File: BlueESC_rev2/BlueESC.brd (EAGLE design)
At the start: 24.4 x 36 mm, 76 parts, among them Q1 BC817-40W, Q2 BC817-40W, Q3 BC817-40W, Q4 SI7370, Q5 SI7370, Q6 SI7370, Q7 SI7370, Q8 SI7370, Q9 SI7370, U1 ATMEGA168MLF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

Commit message: Placed more components on board layout.
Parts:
- removed C8: 0.1uF, SparkFun-Capacitors:0603-CAP
- R15, R16: value 1K -> 330
- moved C3 102.2 mm to (20.3, 14.0), flipped to the bottom, turned to 270 degrees
- moved C2 97.4 mm to (15.9, 34.3), flipped to the bottom
- moved C1 94.3 mm to (20.3, 25.4), flipped to the bottom, turned to 270 degrees
- moved D3 90.0 mm to (18.4, 33.7), flipped to the bottom, turned to 270 degrees
- moved D2 87.1 mm to (22.9, 26.0), flipped to the bottom, turned to 180 degrees
- moved D1 79.7 mm to (22.9, 14.6), flipped to the bottom, turned to 180 degrees
- moved R16 75.2 mm to (27.9, 33.0)
- moved U2 73.0 mm to (21.0, 7.62), turned to 270 degrees
- moved C9 72.3 mm to (21.0, 11.4)
- moved R15 67.3 mm to (24.1, 35.6)
- moved C17 59.9 mm to (14.0, 13.3), turned to 180 degrees
- moved R12 57.5 mm to (23.5, 28.6), turned to 90 degrees
- moved C16 55.3 mm to (14.0, 9.53), turned to 180 degrees
- moved R14 53.1 mm to (11.4, 29.2), turned to 270 degrees
- moved C15 51.7 mm to (14.0, 5.71), turned to 180 degrees
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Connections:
- net GND: no longer C8.2
- net VCC5V: no longer C8.1

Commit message: Added ACS71X to the schematic and board layout to measure current.
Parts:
- added C10, C8: 0.1uF, SparkFun-Capacitors:0603-CAP
- added U$15: ACS712, SparkFun-AnalogIC:SO08
- moved LOGO1 90.0 mm to (4.45, 31.8)
- moved U$4 61.1 mm to (3.17, 27.3)
- moved U$2 8.25 mm to (4.45, 5.71), flipped to the top
- moved U$1 8.08 mm to (21.6, 8.26), flipped to the top
- moved U2 5.72 mm to (21.0, 13.3)
- moved C9 5.24 mm to (19.7, 16.5)
- moved C15 3.81 mm to (10.2, 5.71)
- moved C16 3.81 mm to (10.2, 9.53)
- moved R7 1.42 mm to (5.08, 10.2), turned to 180 degrees
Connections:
- new net CURRENT_ADC: U$15.7, U1.19
- new net N$1: C8.1, U$15.6
- new net VBAT+: U$1.P$1, U$15.1, U$15.2
- net GND: now also C10.2, C8.2, U$15.5
- net VBAT: now also U$15.3, U$15.4; no longer U$1.P$1
- net VCC5V: now also C10.1, U$15.8

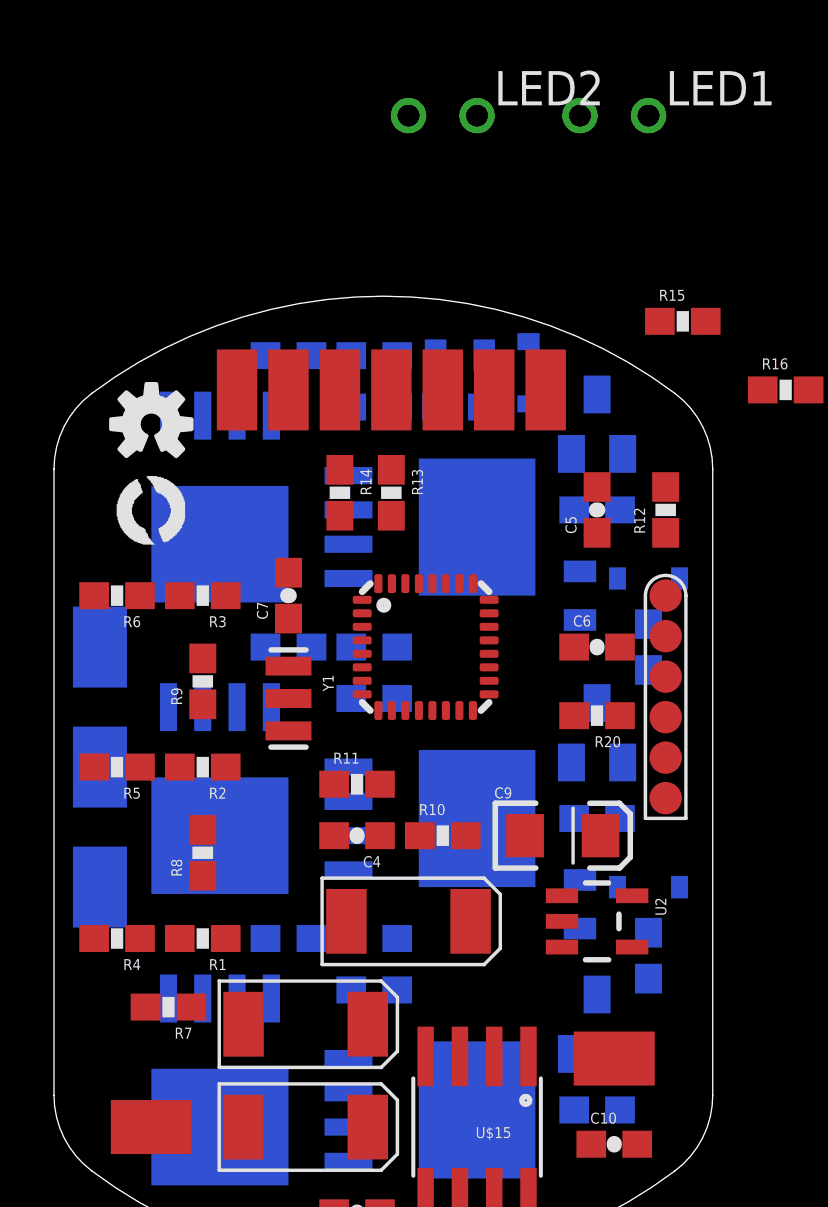
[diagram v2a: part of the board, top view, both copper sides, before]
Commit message: Updated rev3 schematic and split the schematic into two boards.
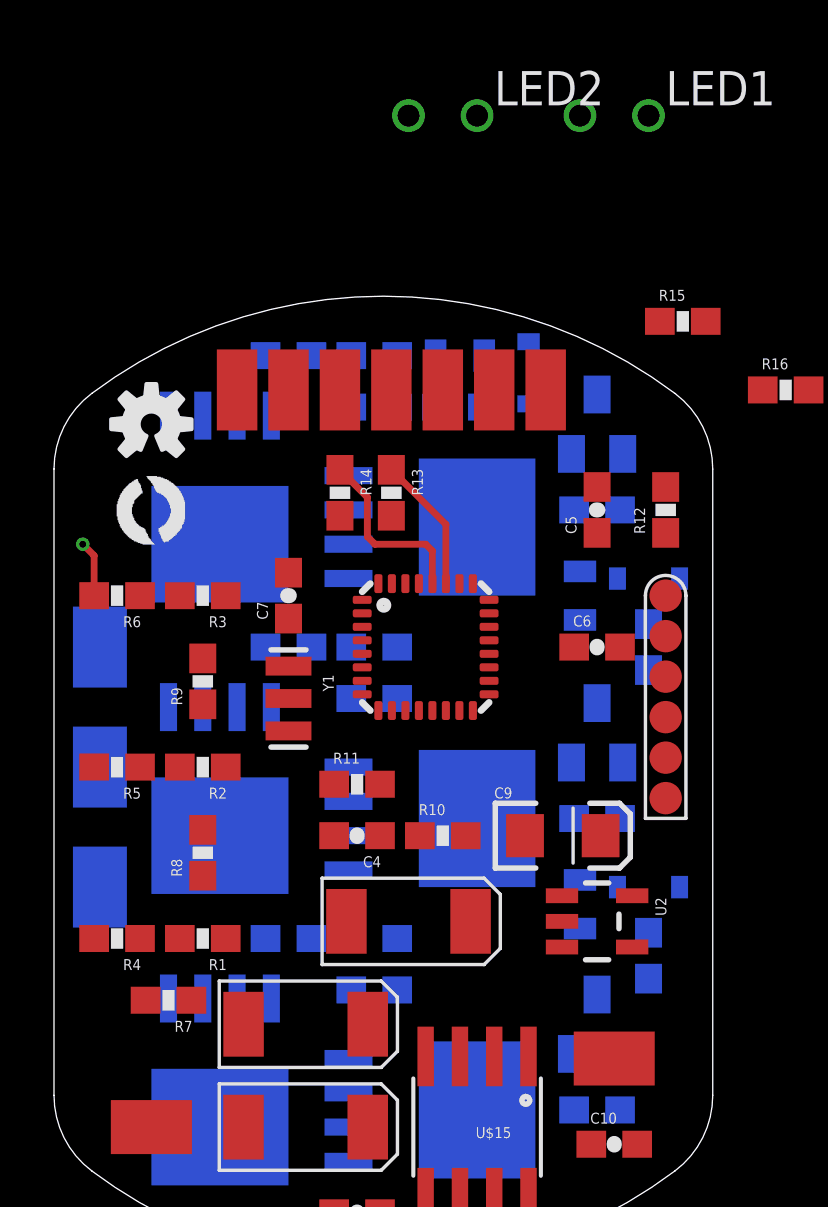
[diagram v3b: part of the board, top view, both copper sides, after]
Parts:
- removed R20: 0, SparkFun-Resistors:0603-RES
- moved R7 0.25 mm to (5.08, 10.4)
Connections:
- removed net MOSI: R20.1, U$14.MOSI
- net PWM_AH: now also U$14.MOSI; no longer R20.2
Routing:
- net SCL: track 0.00 -> 6.73 mm
- net SDA: track 0.00 -> 5.05 mm
- net PHASE_C: track 0.00 -> 4.62 mm, vias 0 -> 1
